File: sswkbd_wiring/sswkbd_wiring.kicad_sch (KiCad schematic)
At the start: 238 parts, among them SW1 SW_PUSH, SW10 SW_PUSH, SW11 SW_PUSH, SW12 SW_PUSH, SW13 SW_PUSH, SW14 SW_PUSH, SW15 SW_PUSH, SW16 SW_PUSH, SW17 SW_PUSH, SW18 SW_PUSH, SW19 SW_PUSH, SW2 SW_PUSH, SW20 SW_PUSH, SW21 SW_PUSH, SW22 SW_PUSH, SW23 SW_PUSH, SW24 SW_PUSH, SW25 SW_PUSH, SW26 SW_PUSH, SW27 SW_PUSH, SW28 SW_PUSH, SW29 SW_PUSH, SW3 SW_PUSH, SW30 SW_PUSH, SW31 SW_PUSH, SW32 SW_PUSH, SW33 SW_PUSH, SW34 SW_PUSH, SW35 SW_PUSH, SW36 SW_PUSH, SW37 SW_PUSH, SW38 SW_PUSH, SW39 SW_PUSH, SW4 SW_PUSH, SW40 SW_PUSH, SW41 SW_PUSH, SW42 SW_PUSH, SW43 SW_PUSH, SW44 SW_PUSH, SW45 SW_PUSH, SW46 SW_PUSH, SW47 SW_PUSH, SW48 SW_PUSH, SW49 SW_PUSH, SW5 SW_PUSH, SW50 SW_PUSH, SW51 SW_PUSH, SW52 SW_PUSH, SW53 SW_PUSH, SW54 SW_PUSH, SW55 SW_PUSH, SW56 SW_PUSH, SW57 SW_PUSH, SW58 SW_PUSH, SW59 SW_PUSH, SW6 SW_PUSH, SW60 SW_PUSH, SW61 SW_PUSH, SW62 SW_PUSH, SW63 SW_PUSH, SW64 SW_PUSH, SW65 SW_PUSH, SW66 SW_PUSH, SW67 SW_PUSH, SW68 SW_PUSH, SW69 SW_PUSH, SW7 SW_PUSH, SW70 SW_PUSH, SW71 SW_PUSH, SW72 SW_PUSH, SW73 SW_PUSH, SW74 SW_PUSH, SW75 SW_PUSH, SW76 SW_PUSH, SW77 SW_PUSH, SW78 SW_PUSH, SW79 SW_PUSH, SW8 SW_PUSH, SW9 SW_PUSH, U1 ProMicro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

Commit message: PCB WIP
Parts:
- added J1, J3: Conn_01x04_Socket, Connector_PinHeader_2.54mm:PinHeader_1x04_P2.54mm_Vertical, symbol Connector:Conn_01x04_Socket
- added J2: USB_SPLIT, Connector_PinHeader_2.54mm:PinHeader_1x04_P2.54mm_Vertical, symbol Connector:Conn_01x04_Socket
- added J4: Conn_01x02_Socket, Connector_PinHeader_2.54mm:PinHeader_1x02_P2.54mm_Vertical, symbol Connector:Conn_01x02_Socket
- added SW80, SW81: SW_Push, Connector_PinHeader_2.54mm:PinHeader_1x02_P2.54mm_Vertical, symbol Switch:SW_Push
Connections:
- net GND: now also J1.4 (Pin_4), J2.1 (Pin_1), SW80.1
- net GND2: now also J3.1 (Pin_1), SW81.1
- net OLED_SCL: now also J1.2 (Pin_2)
- net OLED_SDA: now also J1.1 (Pin_1)
- net RST: now also SW80.2
- net RST_R: now also SW81.2
- net SPLIT_L: now also J2.2 (Pin_2)
- net SPLIT_R: now also J3.2 (Pin_2)
- net VCC: now also J1.3 (Pin_3), J2.4 (Pin_4)
- net VCC2: now also J3.4 (Pin_4)
- net at SW15.A: now also J4.2 (Pin_2)
- net at SW15.B: now also J4.1 (Pin_1)

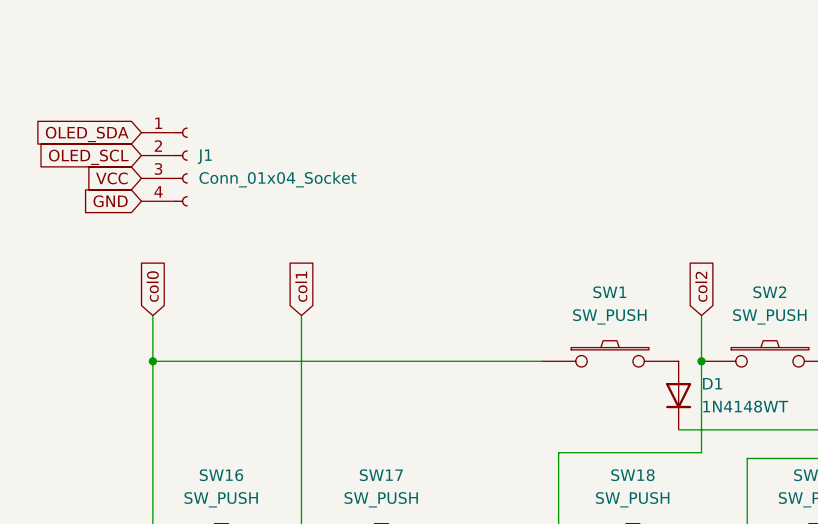
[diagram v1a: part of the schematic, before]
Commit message: PCB silkscreen
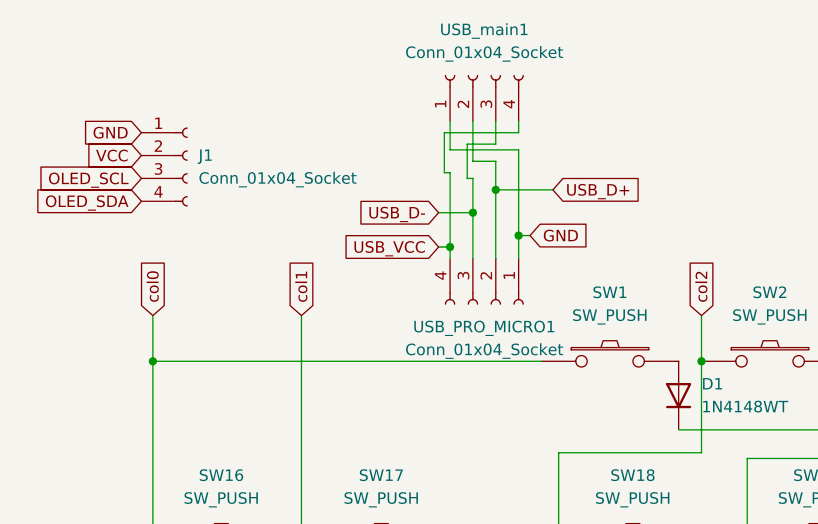
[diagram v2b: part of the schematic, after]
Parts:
- added USB_PRO_MICRO1, USB_main1: Conn_01x04_Socket, Connector_PinHeader_2.54mm:PinHeader_1x04_P2.54mm_Vertical, symbol Connector:Conn_01x04_Socket
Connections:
- net GND: now also J1.1 (Pin_1), USB_PRO_MICRO1.1 (Pin_1), USB_main1.1 (Pin_1); no longer J1.4 (Pin_4)
- net OLED_SCL: now also J1.3 (Pin_3); no longer J1.2 (Pin_2)
- net OLED_SDA: now also J1.4 (Pin_4); no longer J1.1 (Pin_1)
- net VCC: now also J1.2 (Pin_2); no longer J1.3 (Pin_3)
- new net USB_D+: USB_PRO_MICRO1.2 (Pin_2), USB_main1.2 (Pin_2)
- new net USB_D-: USB_PRO_MICRO1.3 (Pin_3), USB_main1.3 (Pin_3)
- new net USB_VCC: USB_PRO_MICRO1.4 (Pin_4), USB_main1.4 (Pin_4)

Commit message: Edge cut WIP
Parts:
- SW16, SW17: footprint MX_Only:MXOnly-1U-Hotswap -> MX_Only:MXOnly-1U-NoLED
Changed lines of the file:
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@@
 			)
 		)
-		(property "Footprint" "MX_Only:MXOnly-1U-Hotswap"
+		(property "Footprint" "MX_Only:MXOnly-1U-NoLED"
 			(at 52.07 71.12 0)
 			(effects
@@
 			)
 		)
-		(property "Footprint" "MX_Only:MXOnly-1U-Hotswap"
+		(property "Footprint" "MX_Only:MXOnly-1U-NoLED"
 			(at 34.29 71.12 0)
 			(effects

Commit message: WIP
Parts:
- renumbered LED27 to LED26, LED26 to LED27, LED36 to LED35, LED35 to LED36, LED56 to LED55, LED55 to LED56, LED66 to LED65, LED65 to LED66
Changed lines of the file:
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@@
 		(dnp no)
 		(fields_autoplaced yes)
-		(property "Reference" "LED56"
+		(property "Reference" "LED55"
 			(at 322.58 190.9111 90)
 			(effects
@@
 			(project "sswkbd"
 				(path "/39bfc9cb-01e5-4e02-98eb-06aab6399778"
-					(reference "LED56")
+					(reference "LED55")
 					(unit 1)
 				)
@@
 		(dnp no)
 		(fields_autoplaced yes)
-		(property "Reference" "LED26"
+		(property "Reference" "LED27"
 			(at 151.13 174.4011 90)
 			(effects
@@
 			(project "sswkbd"
 				(path "/39bfc9cb-01e5-4e02-98eb-06aab6399778"
-					(reference "LED26")
+					(reference "LED27")
 					(unit 1)
 				)
@@
 		(dnp no)
 		(fields_autoplaced yes)
-		(property "Reference" "LED65"
+		(property "Reference" "LED66"
 			(at 287.02 160.4311 90)
 			(effects
@@
 			(project "sswkbd"
 				(path "/39bfc9cb-01e5-4e02-98eb-06aab6399778"
-					(reference "LED65")
+					(reference "LED66")
 					(unit 1)
 				)
@@
 		(dnp no)
 		(fields_autoplaced yes)
-		(property "Reference" "LED27"
+		(property "Reference" "LED26"
 			(at 151.13 189.6411 90)
 			(effects
@@
 			(project "sswkbd"
 				(path "/39bfc9cb-01e5-4e02-98eb-06aab6399778"
-					(reference "LED27")
+					(reference "LED26")
 					(unit 1)
 				)
@@
 		(dnp no)
 		(fields_autoplaced yes)
-		(property "Reference" "LED55"
+		(property "Reference" "LED56"
 			(at 322.58 175.6711 90)
 			(effects
@@
 			(project "sswkbd"
 				(path "/39bfc9cb-01e5-4e02-98eb-06aab6399778"
-					(reference "LED55")
+					(reference "LED56")
 					(unit 1)
 				)
@@
 		(dnp no)
 		(fields_autoplaced yes)
-		(property "Reference" "LED36"
+		(property "Reference" "LED35"
 			(at 186.69 189.6411 90)
 			(effects
@@
 			(project "sswkbd"
 				(path "/39bfc9cb-01e5-4e02-98eb-06aab6399778"
-					(reference "LED36")
+					(reference "LED35")
 					(unit 1)
 				)
@@
 		(dnp no)
 		(fields_autoplaced yes)
-		(property "Reference" "LED66"
+		(property "Reference" "LED65"
 			(at 287.02 175.6711 90)
 			(effects
@@
 			(project "sswkbd"
 				(path "/39bfc9cb-01e5-4e02-98eb-06aab6399778"
-					(reference "LED66")
+					(reference "LED65")
 					(unit 1)
 				)
@@
 		(dnp no)
 		(fields_autoplaced yes)
-		(property "Reference" "LED35"
+		(property "Reference" "LED36"
 			(at 186.69 174.4011 90)
 			(effects
@@
 			(project "sswkbd"
 				(path "/39bfc9cb-01e5-4e02-98eb-06aab6399778"
-					(reference "LED35")
+					(reference "LED36")
 					(unit 1)
 				)
